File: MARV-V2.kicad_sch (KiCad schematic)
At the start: 0 parts

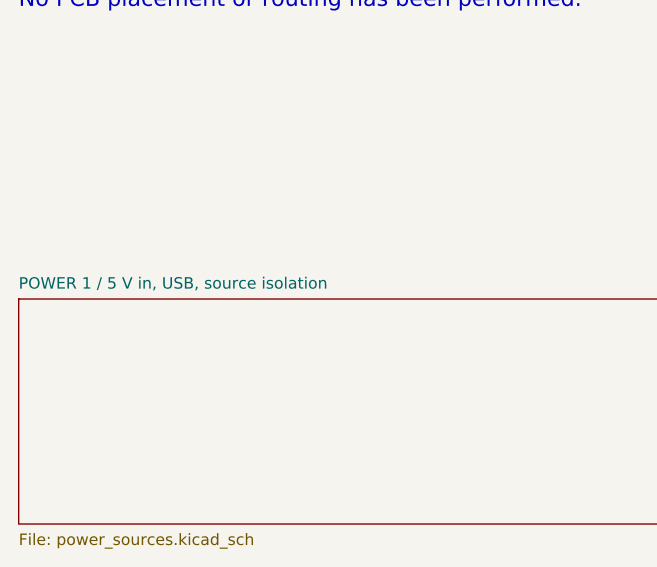
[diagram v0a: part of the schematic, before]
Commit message: Schematic review: TPS2121 input stage, DS-009 ports, sequencing and CS fixes; docs trimmed
Datasheet-grounded review of the full flight-controller schematic. Downstream
of the input everything verified pin-by-pin (TPS62913, TPS7A20, RP2354B,
BMI088/BMP581/ADXL375, W25Q128, microSD, PWM). The 5 V input stage did not:

- LM66100 (5.5 V rec-op / 6 V abs-max) replaced by one TPS2121 mux (U25):
  BEC priority on IN1, OV lockout ~5.86 V, current limit ~1.5 A, reverse
  blocking on both inputs, source status on GPIO39. Input spec 4.75-5.5 V.
- 5V_IN: 2x4.7 uF + 100 uF + SMAJ5.0A TVS; J3 JST-XH -> XT30PW-M (pin 1 GND).
- J6/J7/J9 reordered to Pixhawk DS-009 (VCC/sig/sig/GND); GPS/ELRS VCC 5 V.
- VIN_SENSE 22k/10k (full scale 10.6 V, was saturating at 5.5 V).
- TPS7A20 EN <- PWR_GOOD so V3V3_ANA rises after V3V3_SYS.
- RP2354B VREG_AVDD moved to V3V3_SYS (datasheet 6.1.8: must power up with
  VREG_VIN); ADC_AVDD stays on V3V3_ANA.
- 10k pull-ups on the four sensor chip-selects.
- ERC "global label appears once" re-enabled (0 hits).

Generator, netlist checker and SPICE decks updated (TPS2121 behavioral model,
new over-voltage and 2S mis-plug corners). Build idempotent, 143 pin mappings
PASS, ERC 0/0, all corners PASS.

Docs: POWER_*.md history removed, rationale folded into DESIGN_SPEC Decisions;
808 -> 290 lines across README, DESIGN_SPEC, LIBRARIES, simulations/README.

Co-Authored-By: Claude Fable 5.1 <noreply@anthropic.com>
Claude-Session: https://claude.ai/code/session_015cFNiWgf35VN2T43HaK8PE
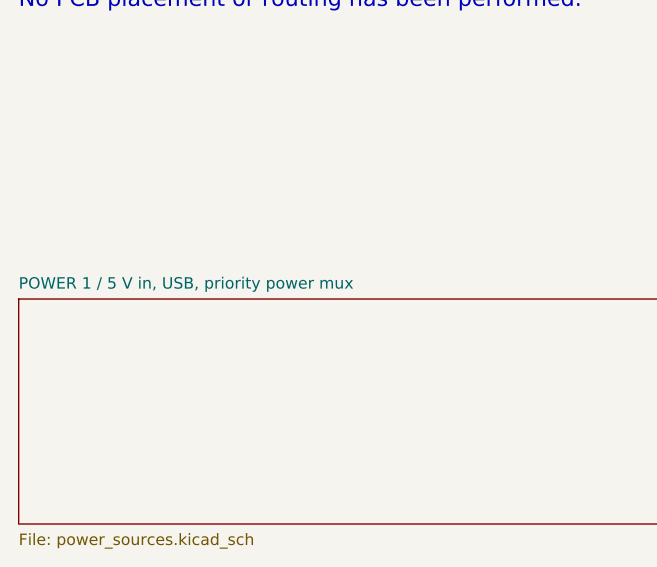
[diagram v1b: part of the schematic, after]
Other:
- sheet POWER 1 / 5 V in, USB, source isolation renamed POWER 1 / 5 V in, USB, priority power mux

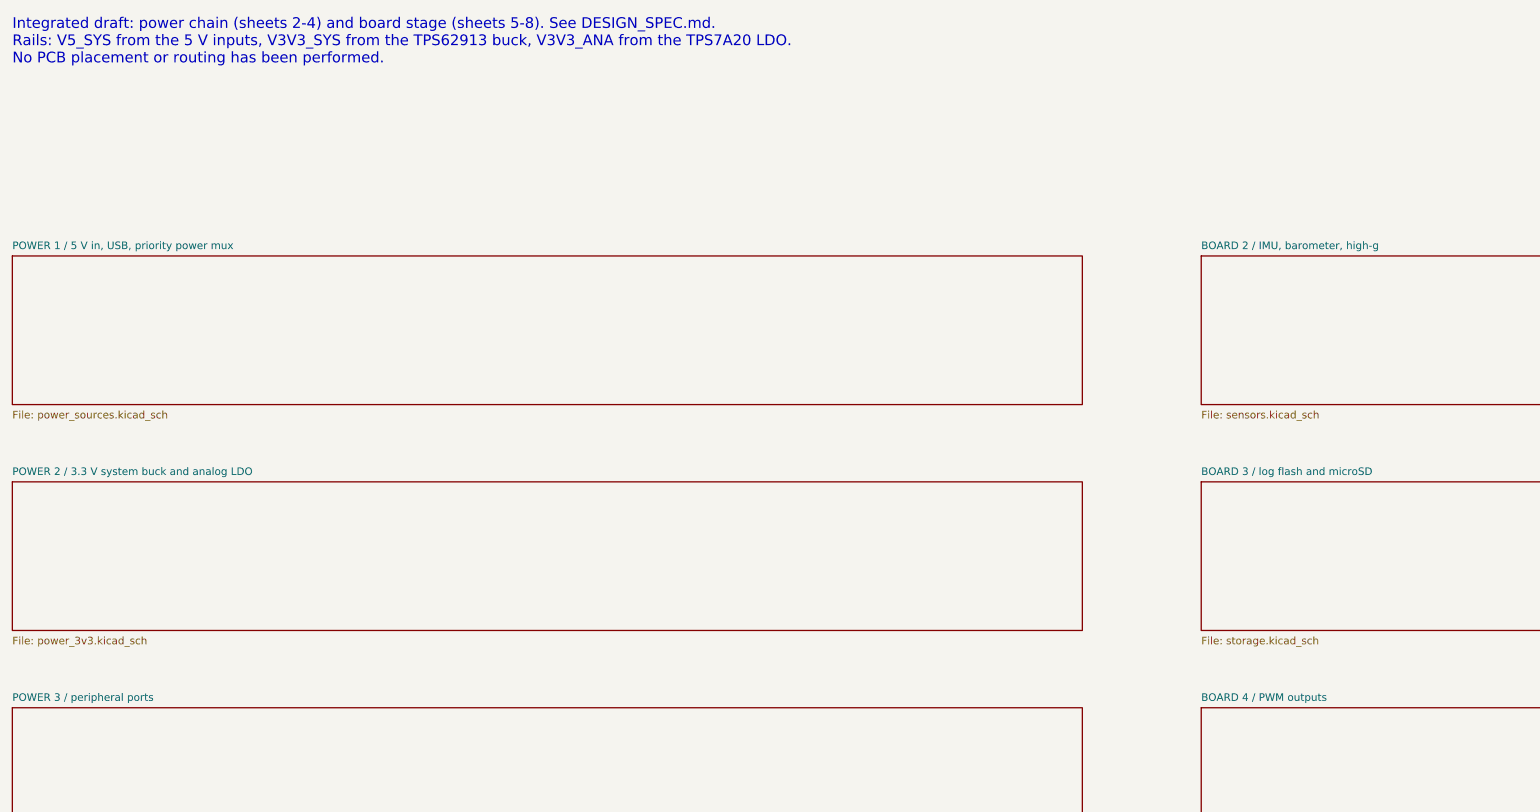
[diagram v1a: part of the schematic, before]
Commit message: Physical design: VBAT-in buck, ESC pad row, pad-row IO, 50 mm single-sided board
Power: the FC now takes raw 2-6S VBAT from the MicoAir AM32 4-in-1 ESC pad
row (CURR TX M4 M3 M2 M1 VBAT GND, J3) through an AP63205WU 5 V/2 A buck
(U26, XGL4030-472, 3 x 22 uF) into the existing TPS2121 mux; XT30 and its
TVS removed. VBAT sense 100k/10k (36 V FS) on ADC0, ESC current sense on
ADC2, ESC KISS telemetry on GPIO30.

IO per the physical spec (DESIGN_SPEC "Physical design"): solder pad rows
for GPS/ELRS/MAG (JST-GH removed), DBG and buzzer; 3x4 servo block for
PWM5-8; 2x6 spare-IO block; WS2812C-2020 RGB LED replaces the two discrete
LEDs; buzzer moved off-board to pads; flash socket is the 150-mil SOIC-8
(W25Q64 default, APS6404L PSRAM alternative); four 4.0 mm grommet holes on
the 30.5 mm pattern. Passives moved to 0402/0603 for the single-sided
envelope.

Board: tools/setup_pcb.py regenerates MARV-V2.kicad_pcb from the netlist —
50 x 50 mm, 4-layer JLC 7628 stack-up, net classes incl. a 90 ohm USB pair,
edge-anchored connectors, coarse interior placement, silk pad labels.
DRC leaves only unrouted items. The BMP581 project footprint had its 2-pad
edges at +/-0.5 mm (corner pads overlapped, three nets shorted); corrected
to Bosch Fig. 32 (+/-0.25 mm, 0.20 mm gaps).

Checks: ERC 0/0, 217 pin mappings / 139 components, run_power_checks PASS,
audit 139/139, pcb DRC unrouted-only.

Co-Authored-By: Claude Fable 5.1 <noreply@anthropic.com>
Claude-Session: https://claude.ai/code/session_01U6Ud7JA3CDTJZVcZZr5sx1
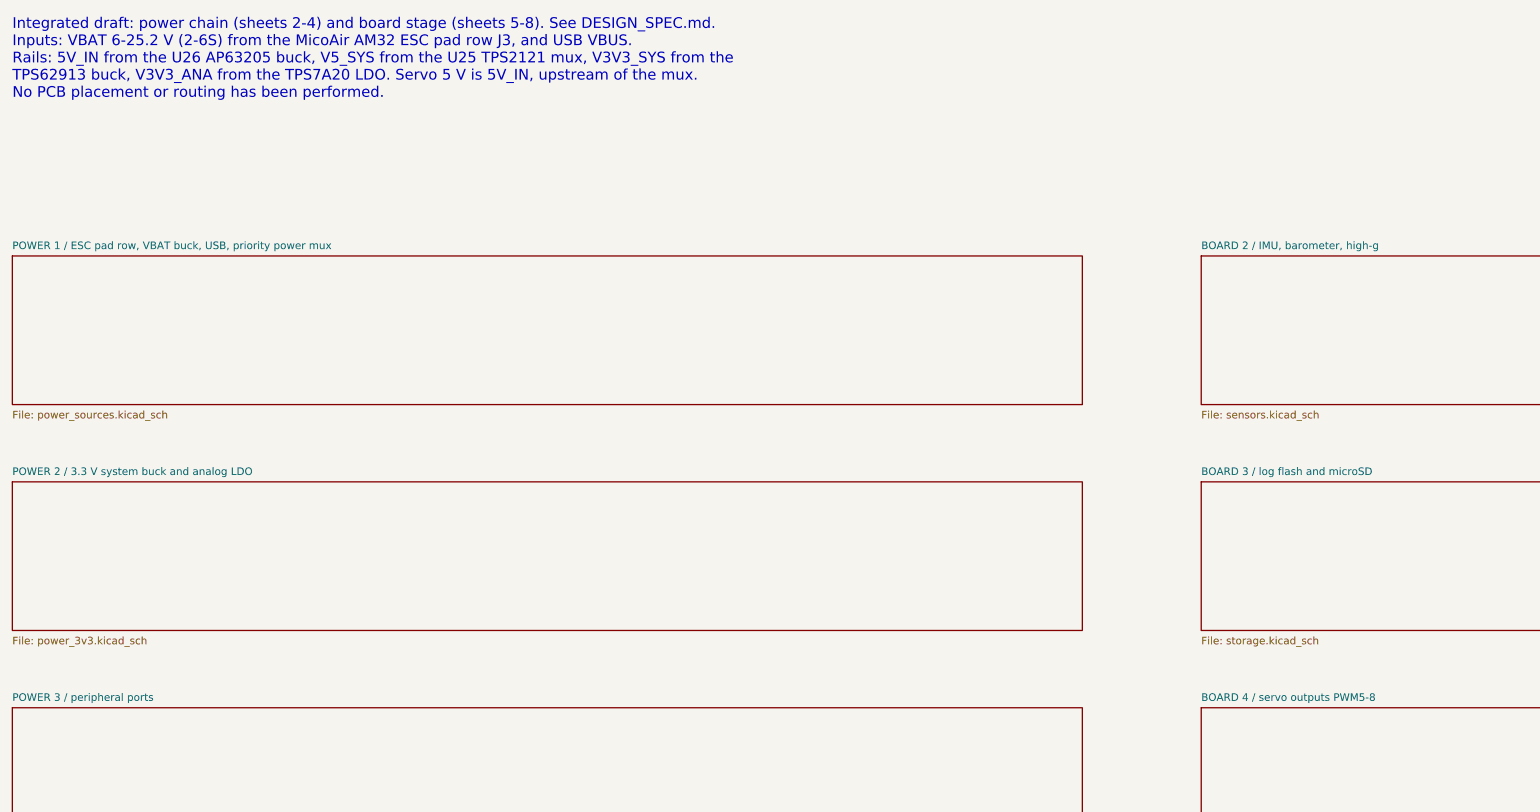
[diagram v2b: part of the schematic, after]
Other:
- sheet BOARD 4 / PWM outputs renamed BOARD 4 / servo outputs PWM5-8
- sheet POWER 1 / 5 V in, USB, priority power mux renamed POWER 1 / ESC pad row, VBAT buck, USB, priority power mux
- note added: "Integrated draft: power chain (sheets 2-4) and board stage (sheets 5-8). See DESIGN_SPEC.md. Inputs: VBAT 6-25.2 V (2-6S) from the MicoAir AM32 ESC pad row J3, and USB VBUS. Rails: 5V_IN from the U26 AP63205 buck, V5_SYS from the U25 TPS2121 mux, V3V3_SYS from the TPS62913 buck, V3V3_ANA from the TPS7A20 LDO. Servo 5 V is 5V_IN, upstream of the mux. No PCB placement or routing has been performed."
- note removed: "Integrated draft: power chain (sheets 2-4) and board stage (sheets 5-8). See DESIGN_SPEC.md. Rails: V5_SYS from the 5 V inputs, V3V3_SYS from the TPS62913 buck, V3V3_ANA from the TPS7A20 LDO. No PCB placement or routing has been performed."

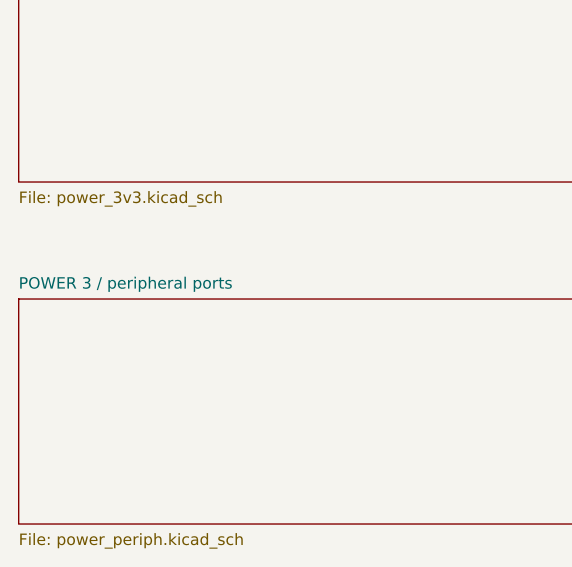
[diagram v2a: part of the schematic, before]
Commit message: IO array replaces bus pad rows; PINOUT.md pin plan; test points; ESC/battery docs
Left edge is now one 2 x 16 through-hole IO array (J6, signal | 5V/3V3/GND
rows, madflight-style) carrying GPS/ELRS/MAG and the ten spare GPIOs; the
J6/J7/J9 pad rows and the J16 block are gone. ESC pad row J3 and DBG pads
J10 stay; servo block J12-J14 stays beside the ESC row. TP1-TP10 1 mm test
points on the sensor SPI, chip selects and interrupts.

PINOUT.md records every GPIO's function and alternates from RP2350
datasheet Table 3, the spare-pin roles (I2C0 on 44/45, SPI1 on 46/47/28,
ADC3-7) and the peripheral ledger; check_power_netlist.py now asserts all
48 GPIO nets against it.

DESIGN_SPEC: ESC connection table, IO array table, test points, battery
monitoring (VBAT_SENSE + ESC current; INA226 rejected), edge allocation.
setup_pcb.py vendors the header footprints with project-local 3D models;
board 50 x 50 mm (48 collides with the grommet keepouts), DRC unrouted-only.
141 components, 105 nets, 231 pin mappings; ERC 0/0, ngspice PASS,
audit 141/141.

Co-Authored-By: Claude Fable 5.1 <noreply@anthropic.com>
Claude-Session: https://claude.ai/code/session_01U6Ud7JA3CDTJZVcZZr5sx1
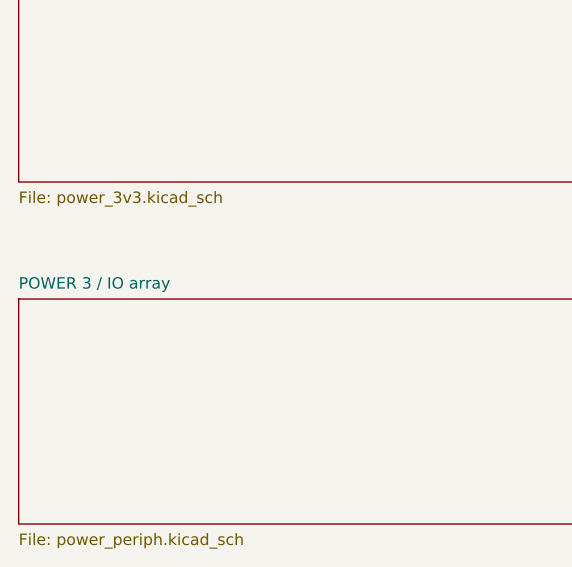
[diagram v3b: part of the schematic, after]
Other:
- sheet POWER 3 / peripheral ports renamed POWER 3 / IO array

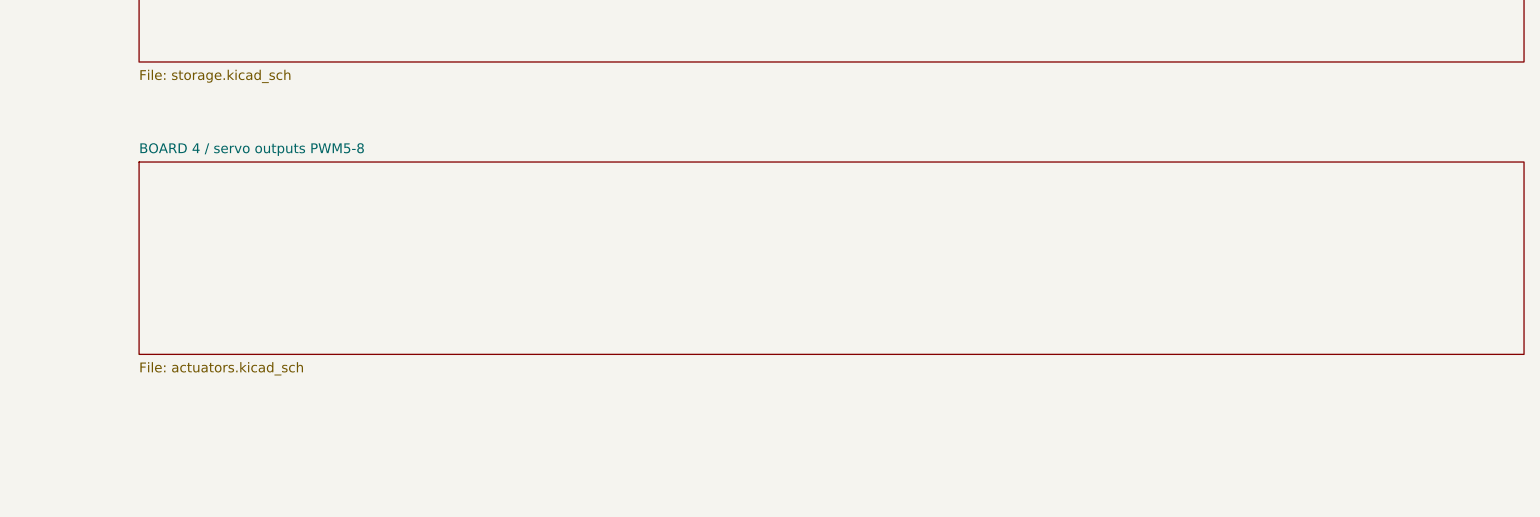
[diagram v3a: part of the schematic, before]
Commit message: Madflight-style layout: 48.7 x 41.2 mm, ESC row left, 3x14 IO block right
Board re-laid out to the madflight FC3v2 arrangement and shrunk from the
50 x 50 square: rectangle 48.7 x 41.2 mm, 30.5 mm mounting square offset
(7.0 mm left margin for the vertical ESC pad row J3, 11.2 mm right margin
for the IO block), grommet keepout Ø6.5. The IO block is three abutting
1x14 rows J6/J7/J8 (signal | 5V/3V3 | GND per row): T0 R0 T1 R1 SDA SCL
S5-S8 A44-A47. The servo block and the 2x16 array are gone (actuators sheet
removed); GPIO 1/21/27/28/31/43 are no-connect (PINOUT.md, checker
updated). microSD ejects off the top edge, USB-C/RESET/BOOT/LED/DBG on the
bottom edge, sensors + test points between the MCU and the IO block.

Courtyard fill 75.7 %, 0 fit/geometry problems, DRC unrouted-only.
140 components; ERC 0/0, checker PASS, ngspice PASS, audit 140/140.
Known: the board-level silk labels on the ESC row and IO block are
mis-nudged by the label fixer (CURR/VBAT/A47 hidden) — silk pass pending.

Co-Authored-By: Claude Fable 5.1 <noreply@anthropic.com>
Claude-Session: https://claude.ai/code/session_01U6Ud7JA3CDTJZVcZZr5sx1
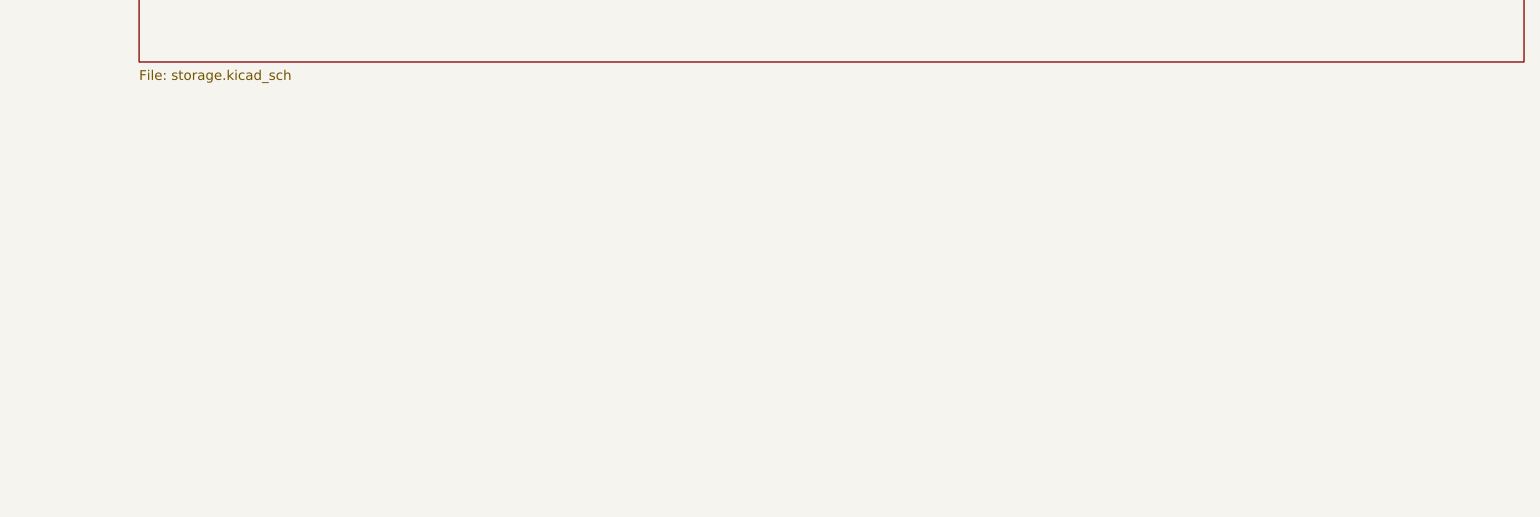
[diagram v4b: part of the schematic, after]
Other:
- removed sheet BOARD 4 / servo outputs PWM5-8

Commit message: Schematic re-organised into 11 per-subsystem pages, drawn as wired blocks
Each subsystem now has its own sheet (RP2354B, USB/debug, ICM-45686, BMP581,
ADXL375, microSD, QSPI expansion, VBAT buck + ESC row, priority mux, 3.3 V
rail, IO block) with the IC's own decoupling, pull-ups, test points and
connectors placed beside it and wired, labels only for nets leaving the
block. Root sheet is an index. tools/build_power.py grows a small layout
engine (wire routing, junctions, decoupling ladders, note flow) with
self-checks for dangling wires and multi-net wire islands; the long design
notes are preserved verbatim as module constants.

Purely presentational: netlist fingerprint (tools/netlist_fingerprint.py,
new) is identical before and after, ERC 0, power checks pass. PCB footprint
paths re-pointed at the new sheet UUIDs by tools/relink_pcb_paths.py (new);
the board diff is path lines only, DRC unconnected count unchanged.
README/DESIGN_SPEC sheet lists updated; pre-change sheets and generator in
backups/pre-sheet-reorg-2026-09-16/.

Also carries the uncommitted work that preceded it: PCB routing, plane
stitching and route-analysis tools (tools/route_*.py, stitch_planes.py),
GPIO remap in PINOUT.md / check_power_netlist.py / setup_pcb.py, and the
grommet mounting-hole footprint update.

Co-Authored-By: Claude Fable 5.1 <noreply@anthropic.com>
Claude-Session: https://claude.ai/code/session_01Y51PayhRcgfdi3hVsfn4qg
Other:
- sheet POWER 2 / 3.3 V system buck and analog LDO renamed POWER 3 / 3.3 V system buck and analog LDO
- removed sheet BOARD 2 / IMU, barometer, high-g
- removed sheet BOARD 3 / log flash and microSD
- removed sheet POWER 1 / ESC pad row, VBAT buck, USB, priority power mux
- removed sheet POWER 3 / IO array
- added sheet BOARD 2 / ADXL375 high-g accelerometer (highg.kicad_sch)
- added sheet BOARD 2 / BMP581 barometer (baro.kicad_sch)
- added sheet BOARD 2 / ICM-45686 six-axis IMU (imu.kicad_sch)
- added sheet BOARD 3 / microSD socket (sd.kicad_sch)
- added sheet BOARD 3 / optional QSPI expansion socket (DNP) (qspi_expansion.kicad_sch)
- added sheet BOARD 4 / IO array, status LED, mounting holes (io_block.kicad_sch)
- added sheet BOARD 5 / USB-C, ESD, SWD pads (usb_debug.kicad_sch)
- added sheet POWER 1 / ESC pad row, VBAT and the 5 V buck (power_vbat.kicad_sch)
- added sheet POWER 2 / TPS2121 priority power mux (power_mux.kicad_sch)
- note added: "MARV V2 flight controller - schematic index. One page per subsystem; on each page the IC is drawn with its own decoupling, pull-ups, series resistors, test points and connectors wired to it, and a global label is used only where a net leaves the page. See DESIGN_SPEC.md for the design itself. Inputs: VBAT 6-25.2 V (2-6S) from the MicoAir AM32 ESC pad row J3, and USB VBUS. Rails: 5V_IN from the U2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"
- note removed: "Integrated draft: power chain (sheets 2-4) and board stage (sheets 5-8). See DESIGN_SPEC.md. Inputs: VBAT 6-25.2 V (2-6S) from the MicoAir AM32 ESC pad row J3, and USB VBUS. Rails: 5V_IN from the U26 AP63205 buck, V5_SYS from the U25 TPS2121 mux, V3V3_SYS from the TPS62913 buck, V3V3_ANA from the TPS7A20 LDO. Servo 5 V is 5V_IN, upstream of the mux. No PCB placement or routing has been performed."
- title: MARV integrated power - preliminary -> MARV-V2 - schematic index
